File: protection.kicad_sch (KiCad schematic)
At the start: 11 parts, among them J501 JST XH horiz, J502 Wire Link, Q501 WST4041

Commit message: SH-RPi v2 schematic design
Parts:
- removed J501: JST XH horiz, SH-RPi:Boomelec_XH-2AW_1x02_P2.50mm_Horiz, symbol Connector_Generic:Conn_01x02
- removed J502: Wire Link, SH-RPi:WireLink_1x02_P2.54mm, symbol Connector_Generic:Conn_01x02
- removed R501: 100k, Resistor_SMD:R_0402_1005Metric, symbol Device:R
- added Q701: BC856BS, Package_TO_SOT_SMD:SOT-363_SC-70-6, symbol Transistor_BJT:BC856BS
- added R701, R702: 10k, symbol Device:R
- D702: renamed from D502; value MM3Z8V2 -> BZT52C15S; LCSC C118606 -> C173448
- F701: renamed from F501; value 12H1250C -> 1206T4A63V; LCSC C182444 -> C354899
- Q702: renamed from Q501; value WST4041 -> SI2309CDS-T1-GE3; LCSC C148357 -> C558250; Notes 5P40, WST4041, PJA3441 or equivalent -> (none)
- renumbered C501 to C701, C502 to C702, C503 to C703, D501 to D701, L501 to L701
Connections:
- net GND: now also R701.2, R702.2
- net RP_G: now also Q701.3 (C2), R702.1
- net Vin_EMI: now also Q701.1 (E1)
- net Vin_protected: now also Q701.4 (E2)
- new net: Q701.2 (B1), Q701.5 (B2), Q701.6 (C1), R701.1
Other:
- note added: "Reverse polarity and reverse current protection"
- note removed: "Optional wire link to power the board from NMEA 2000"
- note removed: "Reverse polarity protection"
- moved on the sheet: C701, C702, C703, D701, D702, F701, L701, Q702

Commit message: Assign footprints and part numbers to components
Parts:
- Q701: LCSC (none) -> C417380
- R701, R702: footprint (none) -> Resistor_SMD:R_0402_1005Metric; LCSC (none) -> C25744
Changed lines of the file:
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@@
       (effects (font (size 1.27 1.27)) (justify left))
     )
-    (property "Footprint" "" (id 2) (at 165.862 87.63 90)
+    (property "Footprint" "Resistor_SMD:R_0402_1005Metric" (id 2) (at 165.862 87.63 90)
       (effects (font (size 1.27 1.27)) hide)
     )
@@
       (effects (font (size 1.27 1.27)) hide)
     )
-    (property "LCSC" "" (id 4) (at 167.64 87.63 0)
+    (property "LCSC" "C25744" (id 4) (at 167.64 87.63 0)
       (effects (font (size 1.27 1.27)) hide)
     )
@@
       (effects (font (size 1.27 1.27)) (justify left))
     )
-    (property "Footprint" "" (id 2) (at 198.882 87.63 90)
+    (property "Footprint" "Resistor_SMD:R_0402_1005Metric" (id 2) (at 198.882 87.63 90)
       (effects (font (size 1.27 1.27)) hide)
     )
@@
       (effects (font (size 1.27 1.27)) hide)
     )
-    (property "LCSC" "" (id 4) (at 200.66 87.63 0)
+    (property "LCSC" "C25744" (id 4) (at 200.66 87.63 0)
       (effects (font (size 1.27 1.27)) hide)
     )
@@
     )
     (property "Datasheet" "https://assets.nexperia.com/documents/data-sheet/BC856BS.pdf" (id 3) (at 198.12 69.85 0)
+      (effects (font (size 1.27 1.27)) hide)
+    )
+    (property "LCSC" "C417380" (id 4) (at 198.12 69.85 0)
       (effects (font (size 1.27 1.27)) hide)
     )
@@
       (effects (font (size 1.27 1.27)) hide)
     )
+    (property "LCSC" "C417380" (id 4) (at 170.18 69.85 0)
+      (effects (font (size 1.27 1.27)) hide)
+    )

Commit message: WIP: PCB layout
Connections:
- net RP_B: now reaches Q701.2 (B1), Q701.5 (B2), Q701.6 (C1), R701.1
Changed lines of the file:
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@@
+    (effects (font (size 1.27 1.27)) (justify left bottom))
+  )
+  (label "RP_B" (at 181.61 69.85 0)
     (effects (font (size 1.27 1.27)) (justify left bottom))
   )
@@
     (effects (font (size 1.27 1.27)) (justify left bottom))
   )
+  (label "RP_HS_C" (at 167.64 78.74 180)
+    (effects (font (size 1.27 1.27)) (justify right bottom))
+  )
   (label "RP_G" (at 179.07 62.23 180)

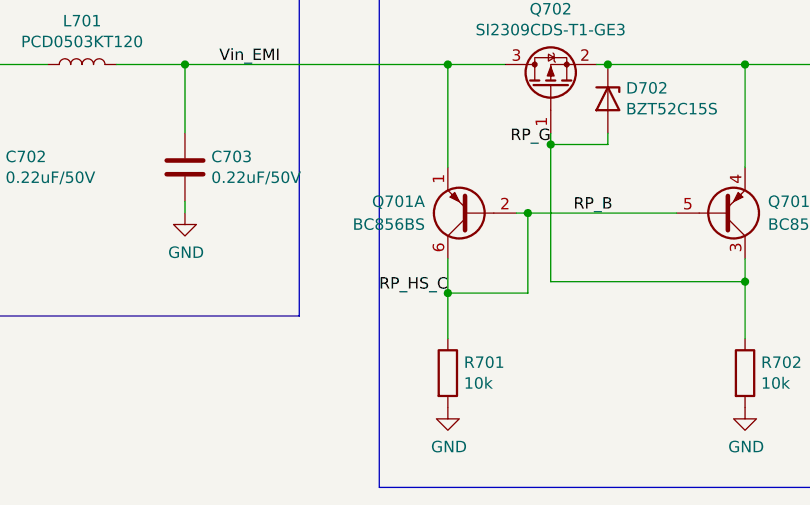
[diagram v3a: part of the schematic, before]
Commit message: Initial PCB component layout done
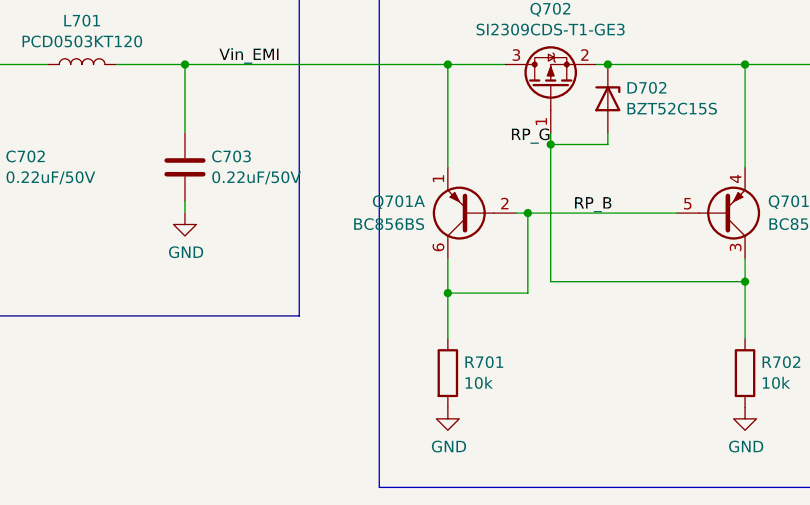
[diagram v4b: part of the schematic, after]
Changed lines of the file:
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@@
     (effects (font (size 1.27 1.27)) (justify left bottom))
-  )
-  (label "RP_HS_C" (at 167.64 78.74 180)
-    (effects (font (size 1.27 1.27)) (justify right bottom))
   )
   (label "RP_G" (at 179.07 62.23 180)

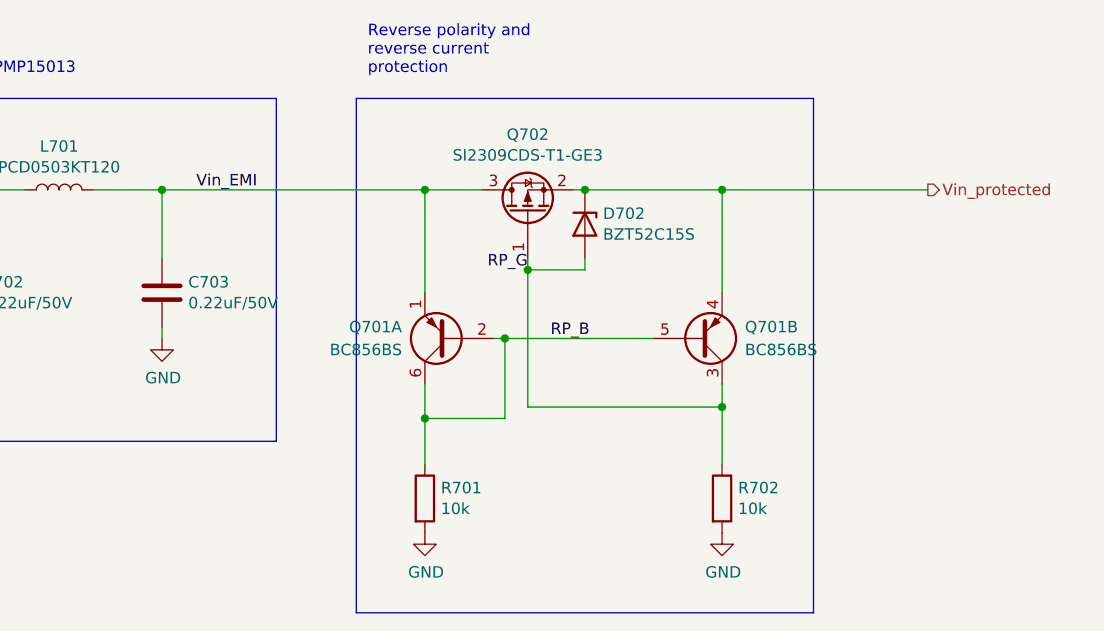
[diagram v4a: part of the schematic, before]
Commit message: Replace "ideal diode" with Schottky & other changes
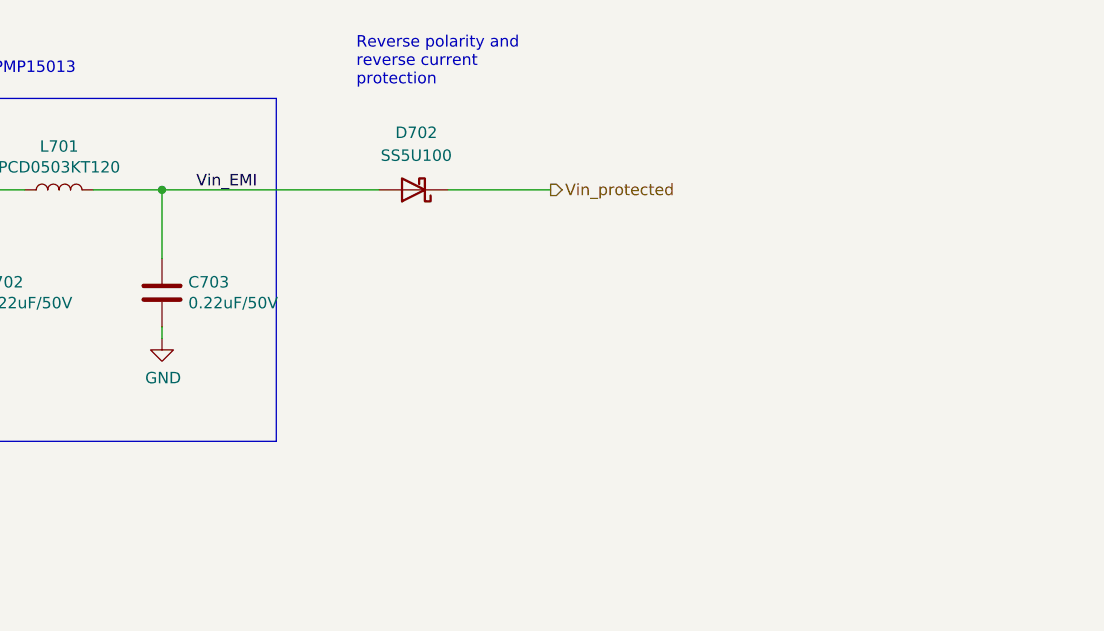
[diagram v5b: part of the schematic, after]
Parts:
- removed D702: BZT52C15S, Diode_SMD:D_SOD-323, symbol Device:D_Zener
- removed Q701: BC856BS, Package_TO_SOT_SMD:SOT-363_SC-70-6, symbol Transistor_BJT:BC856BS
- removed Q702: SI2309CDS-T1-GE3, Package_TO_SOT_SMD:SOT-23, symbol Transistor_FET:Si2371EDS
- removed R701, R702: 10k, Resistor_SMD:R_0402_1005Metric, symbol Device:R
- added D702: SS5U100, SH-RPi:SS5U100_TO-277, symbol Device:D_Schottky
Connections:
- net Vin_EMI: now also D702.2 (A)
- net Vin_protected: now also D702.1 (K)

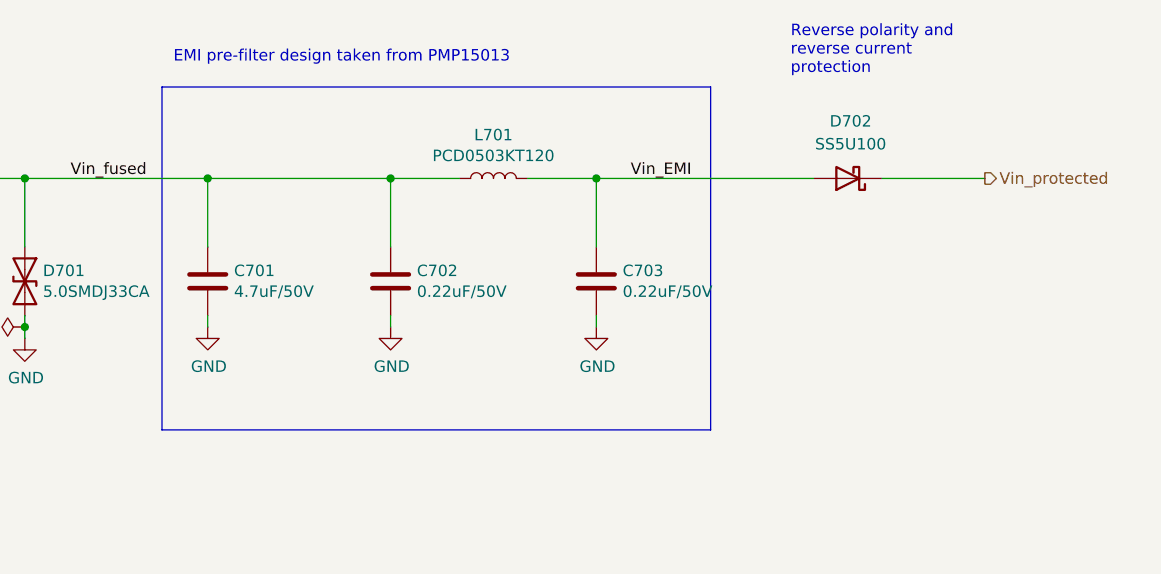
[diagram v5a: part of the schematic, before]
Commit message: Redesign the EMI input filter
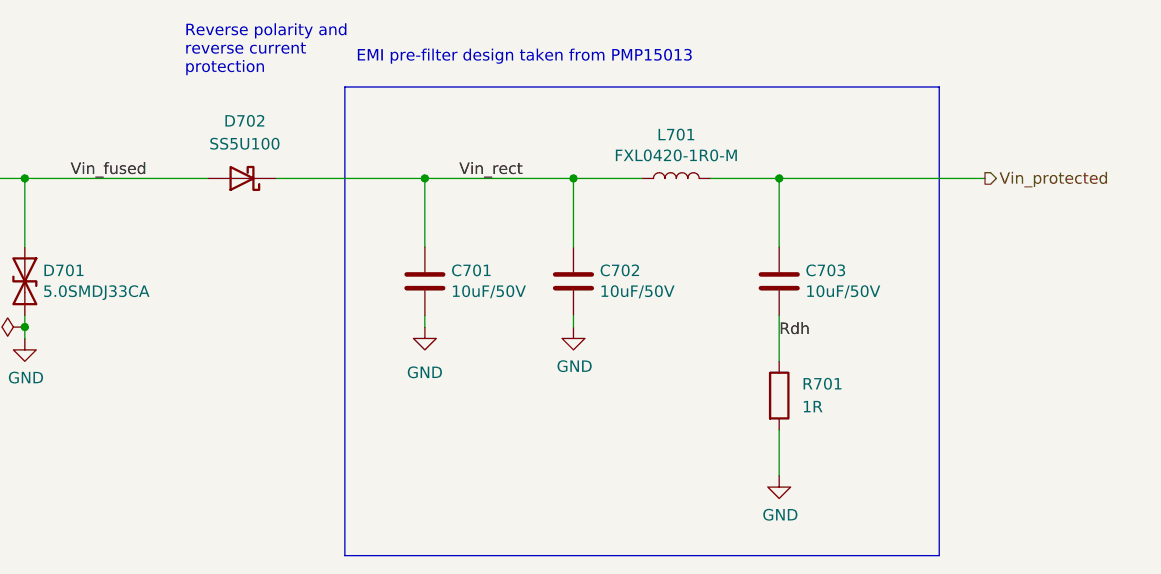
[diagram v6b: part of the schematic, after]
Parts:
- removed C702: 0.22uF/50V, Capacitor_SMD:C_0805_2012Metric, symbol Device:C
- added C701: 10uF/50V, Capacitor_SMD:C_1206_3216Metric, symbol Device:C
- added R701: 1R, Capacitor_SMD:C_0603_1608Metric, symbol Device:R
- C702: renamed from C701; value 4.7uF/50V -> 10uF/50V; LCSC C29823 -> C13585
- C703: value 0.22uF/50V -> 10uF/50V; footprint Capacitor_SMD:C_0805_2012Metric -> Capacitor_SMD:C_1206_3216Metric; LCSC C5378 -> C13585
- L701: value PCD0503KT120 -> FXL0420-1R0-M; footprint SH-RPi:L_PCD0503 -> SH-RPi:L_MWSA0402; LCSC C324292 -> C167203
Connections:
- net GND: now also C701.2, R701.2; no longer C703.2
- net Vin_fused: now also D702.2 (A); no longer C702.1, L701.1
- net Vin_protected: now also C703.1, L701.2; no longer D702.1 (K)
- removed net Vin_EMI: C703.1, D702.2 (A), L701.2
- new net Rdh: C703.2, R701.1
- new net Vin_rect: C701.1, C702.1, D702.1 (K), L701.1
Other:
- moved on the sheet: C702, C703, L701
